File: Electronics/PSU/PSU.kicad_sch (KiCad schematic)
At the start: 11 parts, among them U1 LMR16030SDDA

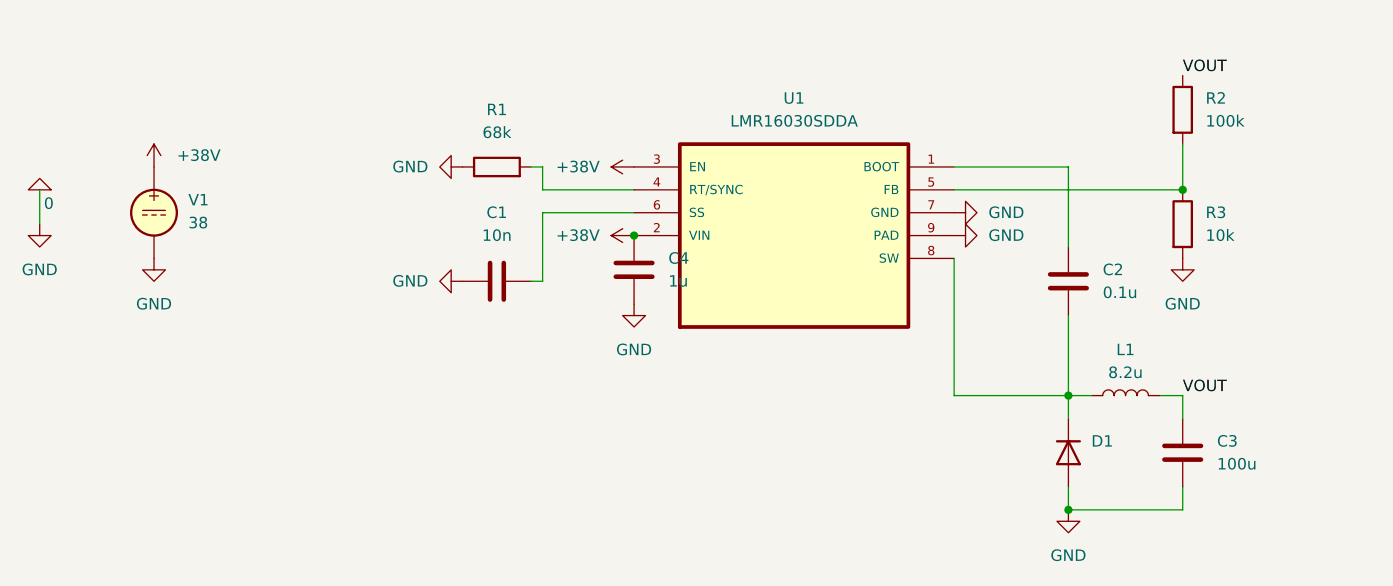
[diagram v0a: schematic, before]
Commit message: Start optimizating the PSU for space
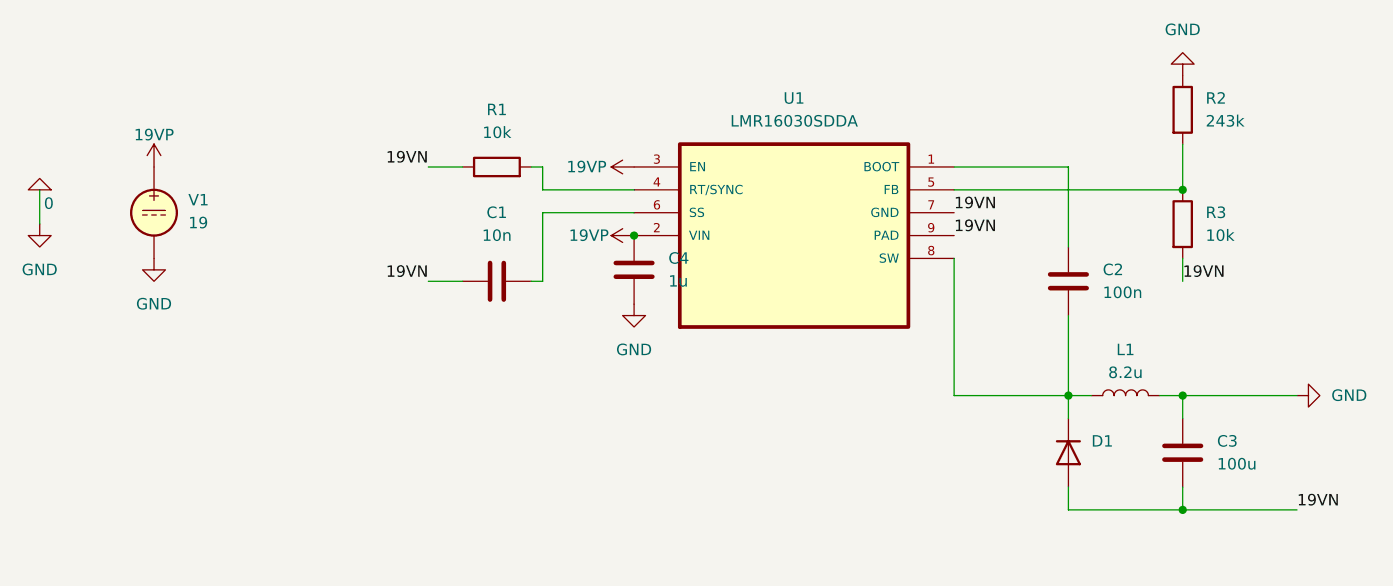
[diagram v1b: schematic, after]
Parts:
- C2: value 0.1u -> 100n
- R1: value 68k -> 10k
- R2: value 100k -> 243k
- V1: value 38 -> 19
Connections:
- net VOUT is gone; now on net 0: C3.1, L1.2, R2.1
- net 0: no longer C1.2, C3.2, D1.2 (A), R1.1, R3.2, U1.7 (GND), U1.9 (PAD)
- net +38V renamed 19VP
- new net 19VN: C1.2, C3.2, D1.2 (A), R1.1, R3.2, U1.7 (GND), U1.9 (PAD)
